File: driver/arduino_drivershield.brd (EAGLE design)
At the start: 60 x 53.7 mm, 37 parts, among them IC1 LB1973M, IC10 LB1973M, IC11 LB1973M, IC12 74HC14D, IC2 LB1973M, IC3 74HC14D, IC4 LB1973M, IC5 LB1973M, IC6 74HC14D, IC7 LB1973M, IC8 LB1973M, IC9 74HC14D, U1 ARDUINO_SHIELDLABEL

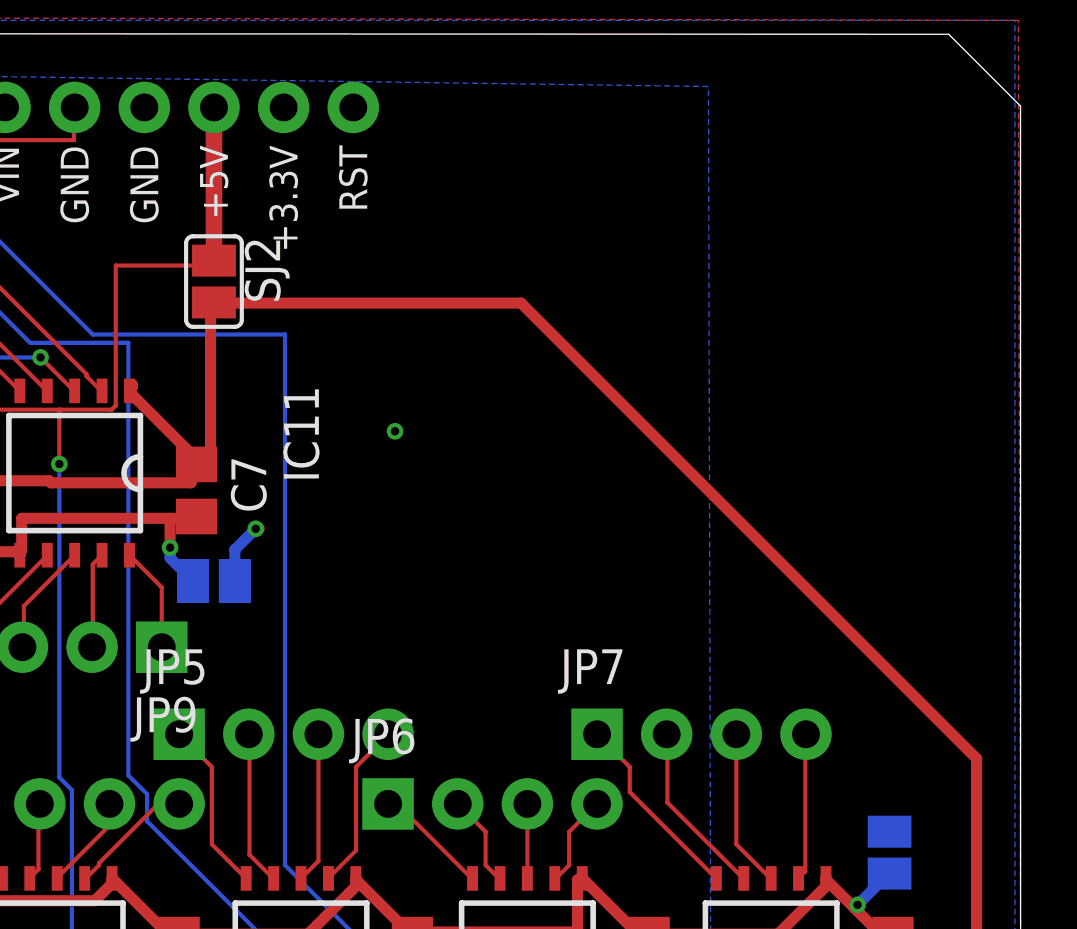
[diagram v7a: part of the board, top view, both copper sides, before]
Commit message: added one more low-ESR cap
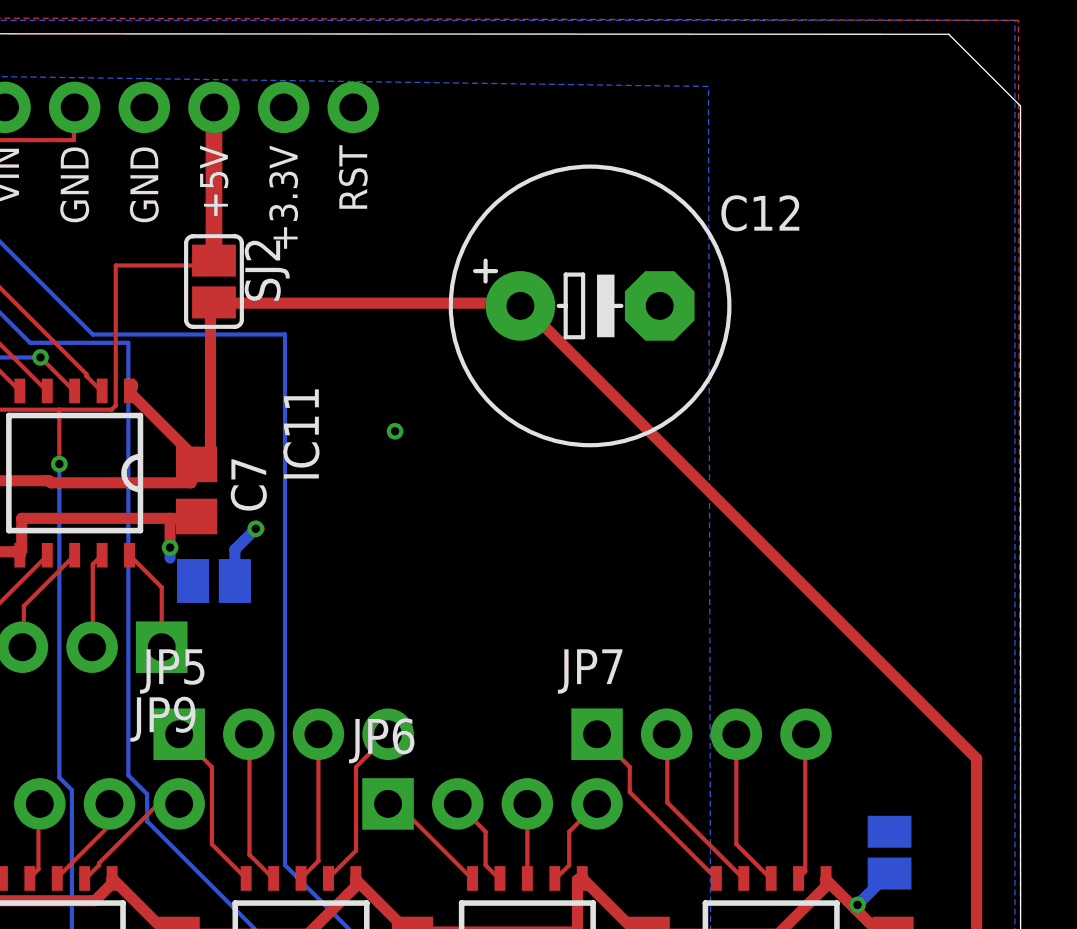
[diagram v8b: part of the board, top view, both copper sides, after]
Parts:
- added C12: 1500uF 6.3V, rcl:E5-10,5
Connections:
- new net GNDA: SJ1.1
- net GND: now also C12.-
- net GND@PWR: no longer SJ1.1
- net V+: now also C12.+
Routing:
- net GND@PWR: track 105.6 -> 104.4 mm
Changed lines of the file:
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@@
 <setting verticaltext="up"/>
 </settings>
-<grid distance="5" unitdist="mil" unit="mil" style="lines" multiple="1" display="yes" altdistance="0.025" altunitdist="inch" altunit="mil"/>
+<grid distance="5" unitdist="mil" unit="mm" style="lines" multiple="1" display="yes" altdistance="0.025" altunitdist="inch" altunit="mil"/>
 <layers>
 <layer number="1" name="Top" color="4" fill="1" visible="yes" active="yes"/>
@@
 <element name="SJ3" library="jumper" package="SJ" value="" x="4.572" y="22.86" rot="MR0"/>
 <element name="SJ4" library="jumper" package="SJ" value="" x="55.118" y="23.622" rot="MR90"/>
+<element name="C12" library="rcl" package="E5-10,5" value="1500uF 6.3V" x="44.196" y="43.561"/>
 </elements>
 <signals>
@@
 <wire x1="5.5626" y1="18.8214" x2="5.715" y2="18.735" width="0.4064" layer="1"/>
 <wire x1="30.48" y1="43.6626" x2="41.6814" y2="43.6626" width="0.4064" layer="1"/>
-<wire x1="41.6814" y1="43.6626" x2="58.293" y2="27.051" width="0.4064" layer="1"/>
+<wire x1="41.6814" y1="43.6626" x2="41.783" y2="43.561" width="0.4064" layer="1"/>
+<wire x1="41.783" y1="43.561" x2="58.293" y2="27.051" width="0.4064" layer="1"/>
 <wire x1="58.293" y1="27.051" x2="58.293" y2="20.64" width="0.4064" layer="1"/>
 <wire x1="58.293" y1="20.64" x2="55.245" y2="18.735" width="0.4064" layer="1"/>
 <wire x1="30.353" y1="43.561" x2="30.353" y2="37.719" width="0.4064" layer="1"/>
+<contactref element="C12" pad="+"/>
+<wire x1="41.656" y1="43.561" x2="41.783" y2="43.561" width="0.4064" layer="1"/>
 <wire x1="30.48" y1="43.6626" x2="30.353" y2="43.561" width="0" layer="19" extent="1-1"/>
 </signal>
@@
 <via x="9.906" y="19.685" extent="1-16" drill="0.3048"/>
 <via x="37.084" y="38.989" extent="1-16" drill="0.3048"/>
+<contactref element="C12" pad="-"/>
 </signal>
 <signal name="5V">
@@
 <signal name="GND@PWR" class="1">
 <contactref element="IC10" pad="6"/>
-<contactref element="SJ1" pad="1"/>
 <contactref element="IC8" pad="6"/>
 <contactref element="IC7" pad="6"/>
@@
 <wire x1="29.7942" y1="35.814" x2="29.845" y2="35.88" width="0.4064" layer="1"/>
 <wire x1="23.4696" y1="34.671" x2="23.4" y2="34.469" width="0.4064" layer="1"/>
-<wire x1="28.8798" y1="34.3662" x2="29.718" y2="33.528" width="0.4064" layer="16"/>
 <wire x1="28.8798" y1="34.7472" x2="28.8798" y2="34.3662" width="0.4064" layer="16"/>
 <wire x1="28.8798" y1="35.814" x2="28.8798" y2="34.7472" width="0.4064" layer="1"/>
@@
 <via x="8.3058" y="33.0708" extent="1-16" drill="0.3048"/>
 </signal>
+<signal name="GNDA">
+<contactref element="SJ1" pad="1"/>
+</signal>
 </signals>
